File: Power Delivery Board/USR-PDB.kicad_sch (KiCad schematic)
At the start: 35 parts, among them U1 XT90, U10 Anderson PP45 Vert. 2x1, U11 Anderson PP45 Vert. 2x1, U12 Anderson PP45 Vert. 2x1, U13 LM2575-5.0BT, U14 MCP3002-I/P, U2 Anderson PP45 Vert. 2x1, U3 Anderson PP45 Vert. 2x1, U4 Anderson PP45 Vert. 2x1, U5 Anderson PP45 Vert. 2x1, U6 Anderson PP45 Vert. 2x1, U7 LM2676T-12_NOPB

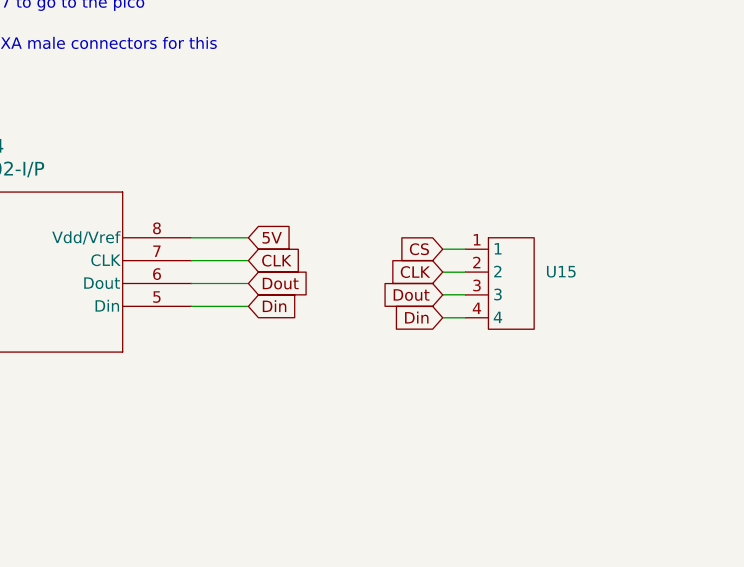
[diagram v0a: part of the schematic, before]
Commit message: fixed typo on PDB schematic
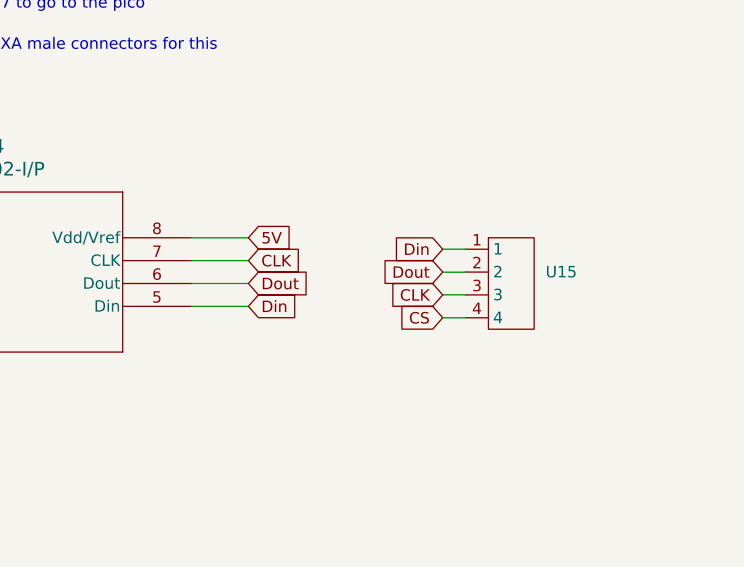
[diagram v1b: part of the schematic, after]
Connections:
- net CLK: now also U15.3; no longer U15.2
- net CS: now also U15.4; no longer U15.1
- net Din: now also U15.1; no longer U15.4
- net Dout: now also U15.2; no longer U15.3

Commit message: updated PDB and analog board
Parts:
- added C8, C9: 10uF, Capacitor_SMD:C_0805_2012Metric_Pad1.18x1.45mm_HandSolder, symbol Device:C_Polarized_US
- added U17: AMS1117-3.3, USR:SOT_AMS1117-2.5_AMS, symbol USR:AMS1117-3.3
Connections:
- net 5V_OUT: now also C8.1, U17.3 (INPUT)
- net GND: now also C8.2, C9.2, U17.1 (ADJ/GND)
- net 5V renamed 3.3V_out
- net 3.3V_out: now also C9.1, U17.2 (OUTPUT), U17.4 (VOUT)
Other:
- note added: "put the 3.3v regulator for ADC chip here (only need to put in the capacitors from the implementation, don't care about diode)"
- note removed: "connect the pins like this GND - 5V - GND"
- note removed: "use the 3-pin JST-XA connectors to route 5V to the backplane"
- moved on the sheet: C5, C6, C7, D2, L2, U13, U16

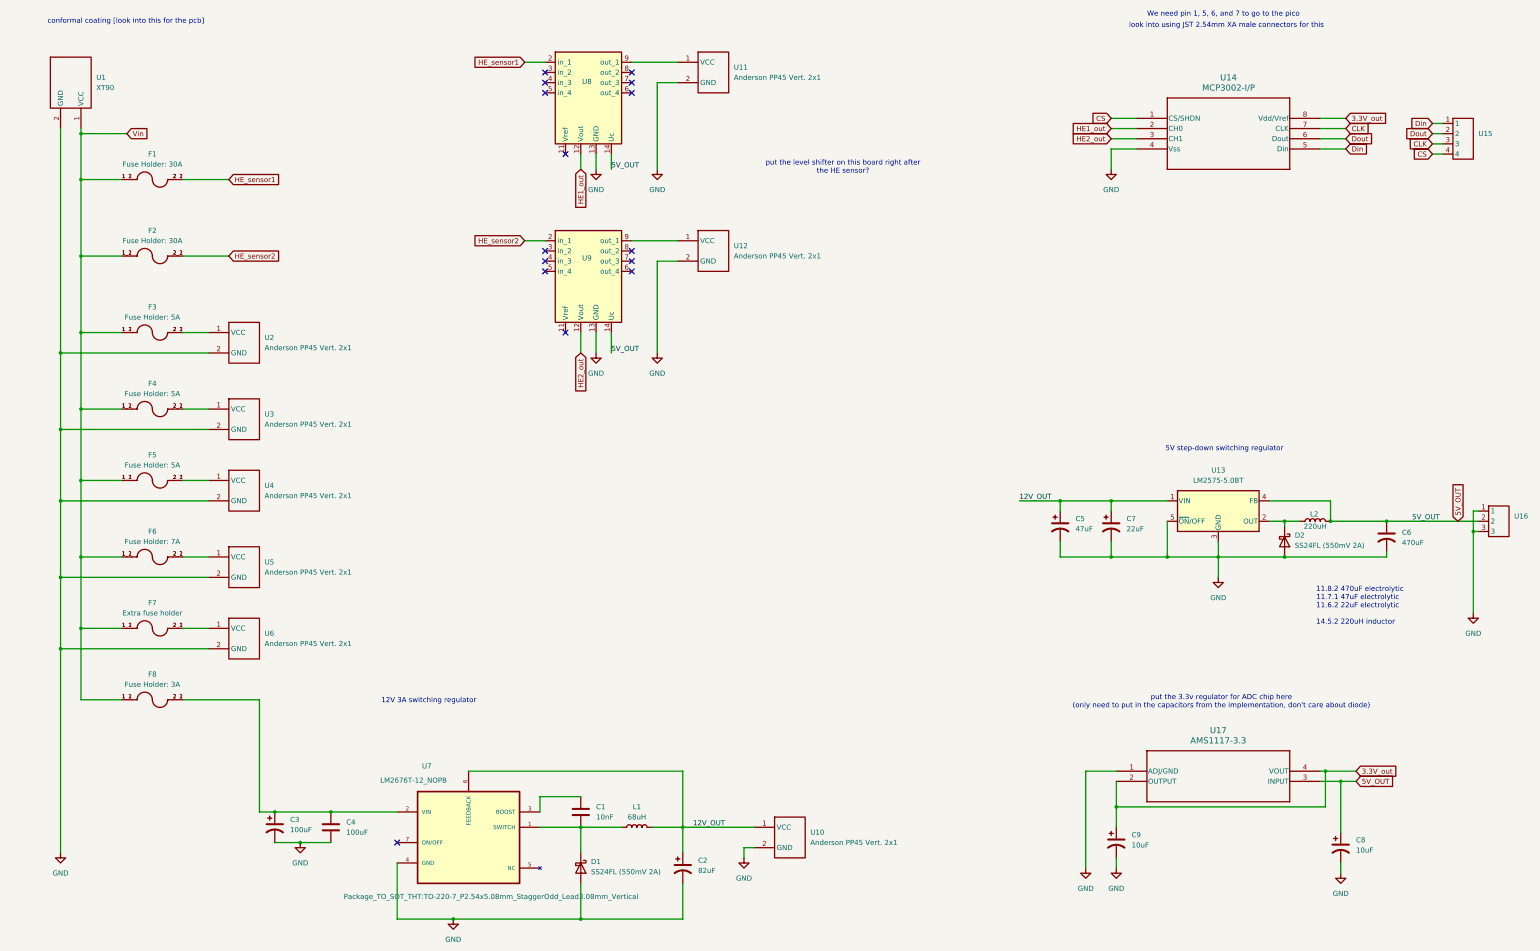
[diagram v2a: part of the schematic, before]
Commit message: replaced LM2575 volt. regulator with 2x LM7805 in parallel
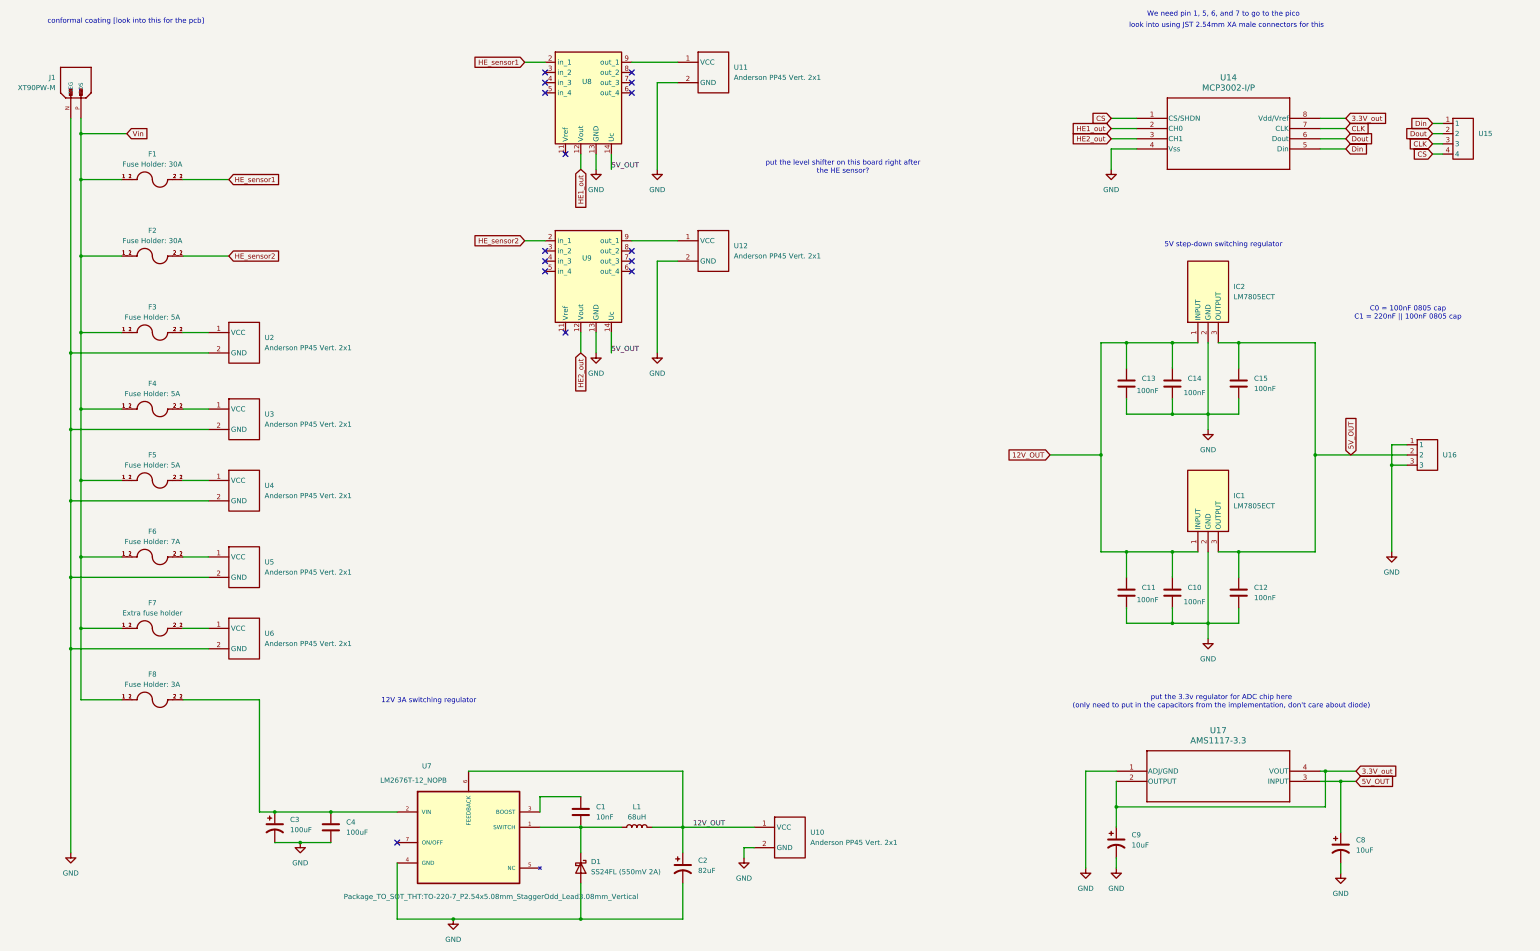
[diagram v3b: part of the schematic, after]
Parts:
- removed C5: 47uF, Capacitor_THT:CP_Radial_D8.0mm_P3.50mm, symbol Device:C_Polarized_US
- removed C6: 470uF, Capacitor_THT:CP_Radial_D8.0mm_P3.50mm, symbol Device:C_US
- removed C7: 22uF, Capacitor_THT:CP_Radial_D8.0mm_P3.50mm, symbol Device:C_Polarized_US
- removed D2: SS24FL (550mV 2A), Diode_THT:D_DO-41_SOD81_P10.16mm_Horizontal, symbol Device:D_Schottky
- removed L2: 220uH, Inductor_THT:L_Axial_L5.3mm_D2.2mm_P10.16mm_Horizontal_Vishay_IM-1, symbol Device:L
- removed U1: XT90, USR:AMASS_XT90PW-M_VERTICAL, symbol USR_SymbolLibrary:root_3_XT90_
- removed U13: LM2575-5.0BT, Package_TO_SOT_THT:TO-220-5_Vertical, symbol Regulator_Switching:LM2575-5.0BT
- added C10, C11, C12, C13, C14, C15: 100nF, Capacitor_SMD:C_0805_2012Metric_Pad1.18x1.45mm_HandSolder, symbol Device:C
- added IC1, IC2: LM7805ECT, USR:LM7805ECT, symbol USR:LM7805ECT
- added J1: XT90PW-M, USR:AMASS_XT90PW-M_VERTICAL, symbol USR:XT90PW-M
- C1: footprint Capacitor_THT:C_Disc_D16.0mm_W5.0mm_P10.00mm -> Capacitor_SMD:C_0805_2012Metric_Pad1.18x1.45mm_HandSolder
- C4: footprint Capacitor_THT:C_Disc_D16.0mm_W5.0mm_P10.00mm -> Capacitor_THT:CP_Radial_D10.0mm_P5.00mm
- U15, U16, U8, U9: value ~ -> (none)
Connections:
- net 12V_OUT: now also C10.1, C11.1, C13.1, C14.1, IC1.1 (INPUT), IC2.1 (INPUT)
- net 5V_OUT: now also C12.1, C15.1, IC1.3 (OUTPUT), IC2.3 (OUTPUT)
- net GND: now also C10.2, C11.2, C12.2, C13.2, C14.2, C15.2, IC1.2 (GND), IC2.2 (GND), J1.N (NEG)
- net Vin: now also J1.P (POS)
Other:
- note added: "C0 = 100nF 0805 cap C1 = 220nF || 100nF 0805 cap"
- note removed: "11.8.2 470uF electrolytic 11.7.1 47uF electrolytic 11.6.2 22uF electrolytic 14.5.2 220uH inductor"

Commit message: Complete redesign of PDB pcb
AAAAAAAAAAAAAAAAAAAAAAAAAAAAAAAAAAAAAAAAAAAA
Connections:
- net HE_sensor1: now also U8.3 (in_2), U8.4 (in_3), U8.5 (in_4)
- net HE_sensor2: now also U9.3 (in_2), U9.4 (in_3), U9.5 (in_4)
- net at U12.1 (VCC), U9.9 (out_1): now also U9.6 (out_4), U9.7 (out_3), U9.8 (out_2)
- net at U8.6 (out_4): now also U11.1 (VCC), U8.7 (out_3), U8.8 (out_2), U8.9 (out_1)
- no-connect marks 15 -> 3
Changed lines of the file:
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@@
+	)
+	(junction
+		(at 147.32 81.28)
+		(diameter 0)
+		(color 0 0 0 0)
 	)
 	(junction
@@
 	)
 	(junction
+		(at 168.91 83.82)
+		(diameter 0)
+		(color 0 0 0 0)
+	)
+	(junction
+		(at 168.91 78.74)
+		(diameter 0)
+		(color 0 0 0 0)
+	)
+	(junction
+		(at 168.91 34.29)
+		(diameter 0)
+		(color 0 0 0 0)
+	)
+	(junction
 		(at 29.21 106.68)
 		(diameter 0)
@@
 	)
 	(junction
+		(at 147.32 36.83)
+		(diameter 0)
+		(color 0 0 0 0)
+	)
+	(junction
 		(at 285.75 132.08)
 		(diameter 0)
@@
 	)
 	(junction
+		(at 147.32 83.82)
+		(diameter 0)
+		(color 0 0 0 0)
+	)
+	(junction
 		(at 289.56 219.71)
 		(diameter 0)
@@
 	)
 	(junction
+		(at 168.91 36.83)
+		(diameter 0)
+		(color 0 0 0 0)
+	)
+	(junction
 		(at 303.53 104.14)
 		(diameter 0)
@@
 	)
 	(junction
+		(at 147.32 78.74)
+		(diameter 0)
+		(color 0 0 0 0)
+	)
+	(junction
 		(at 29.21 143.51)
 		(diameter 0)
@@
 	)
 	(junction
+		(at 147.32 39.37)
+		(diameter 0)
+		(color 0 0 0 0)
+	)
+	(junction
 		(at 31.75 175.26)
 		(diameter 0)
@@
 	)
 	(junction
+		(at 147.32 34.29)
+		(diameter 0)
+		(color 0 0 0 0)
+	)
+	(junction
 		(at 292.1 156.21)
 		(diameter 0)
@@
 	(junction
 		(at 341.63 210.82)
+		(diameter 0)
+		(color 0 0 0 0)
+	)
+	(junction
+		(at 168.91 81.28)
+		(diameter 0)
+		(color 0 0 0 0)
+	)
+	(junction
+		(at 168.91 39.37)
 		(diameter 0)
 		(color 0 0 0 0)
@@
 	)
 	(no_connect
-		(at 147.32 86.36)
-	)
-	(no_connect
-		(at 168.91 86.36)
-	)
-	(no_connect
 		(at 152.4 101.6)
 	)
-	(no_connect
-		(at 147.32 83.82)
-	)
-	(no_connect
-		(at 147.32 36.83)
-	)
-	(no_connect
-		(at 168.91 83.82)
-	)
-	(no_connect
-		(at 147.32 41.91)
-	)
-	(no_connect
-		(at 168.91 39.37)
-	)
-	(no_connect
-		(at 147.32 39.37)
-	)
-	(no_connect
-		(at 147.32 81.28)
-	)
-	(no_connect
-		(at 168.91 81.28)
-	)
-	(no_connect
-		(at 168.91 41.91)
-	)
-	(no_connect
-		(at 168.91 36.83)
+	(wire
+		(pts
+			(xy 168.91 39.37) (xy 168.91 41.91)
+		)
+		(stroke
+			(width 0)
+			(type default)
+		)
 	)
 	(wire
@@
 	(wire
 		(pts
+			(xy 147.32 81.28) (xy 147.32 83.82)
+		)
+		(stroke
+			(width 0)
+			(type default)
+		)
+	)
+	(wire
+		(pts
 			(xy 312.42 156.21) (xy 312.42 173.99)
 		)
@@
 	(wire
 		(pts
+			(xy 168.91 78.74) (xy 168.91 81.28)
+		)
+		(stroke
+			(width 0)
+			(type default)
+		)
+	)
+	(wire
+		(pts
 			(xy 31.75 120.65) (xy 41.91 120.65)
 		)
@@
 	(wire
 		(pts
+			(xy 168.91 83.82) (xy 168.91 86.36)
+		)
+		(stroke
+			(width 0)
+			(type default)
+		)
+	)
+	(wire
+		(pts
 			(xy 180.34 83.82) (xy 175.26 83.82)
 		)
@@
 	(wire
 		(pts
+			(xy 168.91 81.28) (xy 168.91 83.82)
+		)
+		(stroke
+			(width 0)
+			(type default)
+		)
+	)
+	(wire
+		(pts
 			(xy 340.36 213.36) (xy 345.44 213.36)
 		)
@@
 	(wire
 		(pts
+			(xy 168.91 34.29) (xy 168.91 36.83)
+		)
+		(stroke
+			(width 0)
+			(type default)
+		)
+	)
+	(wire
+		(pts
 			(xy 29.21 106.68) (xy 29.21 125.73)
 		)
@@
 	(wire
 		(pts
+			(xy 147.32 78.74) (xy 147.32 81.28)
+		)
+		(stroke
+			(width 0)
+			(type default)
+		)
+	)
+	(wire
+		(pts
 			(xy 31.75 157.48) (xy 41.91 157.48)
 		)
@@
 	(wire
 		(pts
+			(xy 147.32 39.37) (xy 147.32 41.91)
+		)
+		(stroke
+			(width 0)
+			(type default)
+		)
+	)
+	(wire
+		(pts
 			(xy 29.21 143.51) (xy 29.21 162.56)
 		)
@@
 	(wire
 		(pts
+			(xy 147.32 83.82) (xy 147.32 86.36)
+		)
+		(stroke
+			(width 0)
+			(type default)
+		)
+	)
+	(wire
+		(pts
 			(xy 345.44 213.36) (xy 349.25 213.36)
 		)
@@
 	(wire
 		(pts
+			(xy 147.32 34.29) (xy 147.32 36.83)
+		)
+		(stroke
+			(width 0)
+			(type default)
+		)
+	)
+	(wire
+		(pts
 			(xy 196.85 229.87) (xy 199.39 229.87)
 		)
@@
 	(wire
 		(pts
+			(xy 168.91 36.83) (xy 168.91 39.37)
+		)
+		(stroke
+			(width 0)
+			(type default)
+		)
+	)
+	(wire
+		(pts
 			(xy 312.42 104.14) (xy 312.42 121.92)
 		)
@@
 		)
 		(stroke
+			(width 0)
+			(type default)
+		)
+	)
+	(wire
+		(pts
+			(xy 147.32 36.83) (xy 147.32 39.37)
+		)
+		(stroke

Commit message: Final PDB tweaks. New production run.
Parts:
- added U1, U13: (no value), USR:JST-XA 3-PIN, symbol USR:JST-XA_3-PIN
- F3, F4, F5: value Fuse Holder: 5A -> Fuse Holder: 30A
- F6: value Fuse Holder: 7A -> Fuse Holder: 30A
- F7: value Extra fuse holder -> Fuse Holder: 30A
- F8: value Fuse Holder: 3A -> Fuse Holder: 30A
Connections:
- net GND: now also U1.1, U1.3, U13.1, U13.3
- net HE1_out: now also U1.2
- net HE2_out: now also U13.2
